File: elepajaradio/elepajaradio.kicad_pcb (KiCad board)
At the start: 2 copper layers, 29 parts, among them J1 SPI, J2 UART, J3 vdd_gnd, J4 reset, SW1 RotaryEncoder, SW2 SW_Push, SW3 SW_Push, U1 MAX2606, U2 OLED_I2C, U3 ATmega328PB-A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

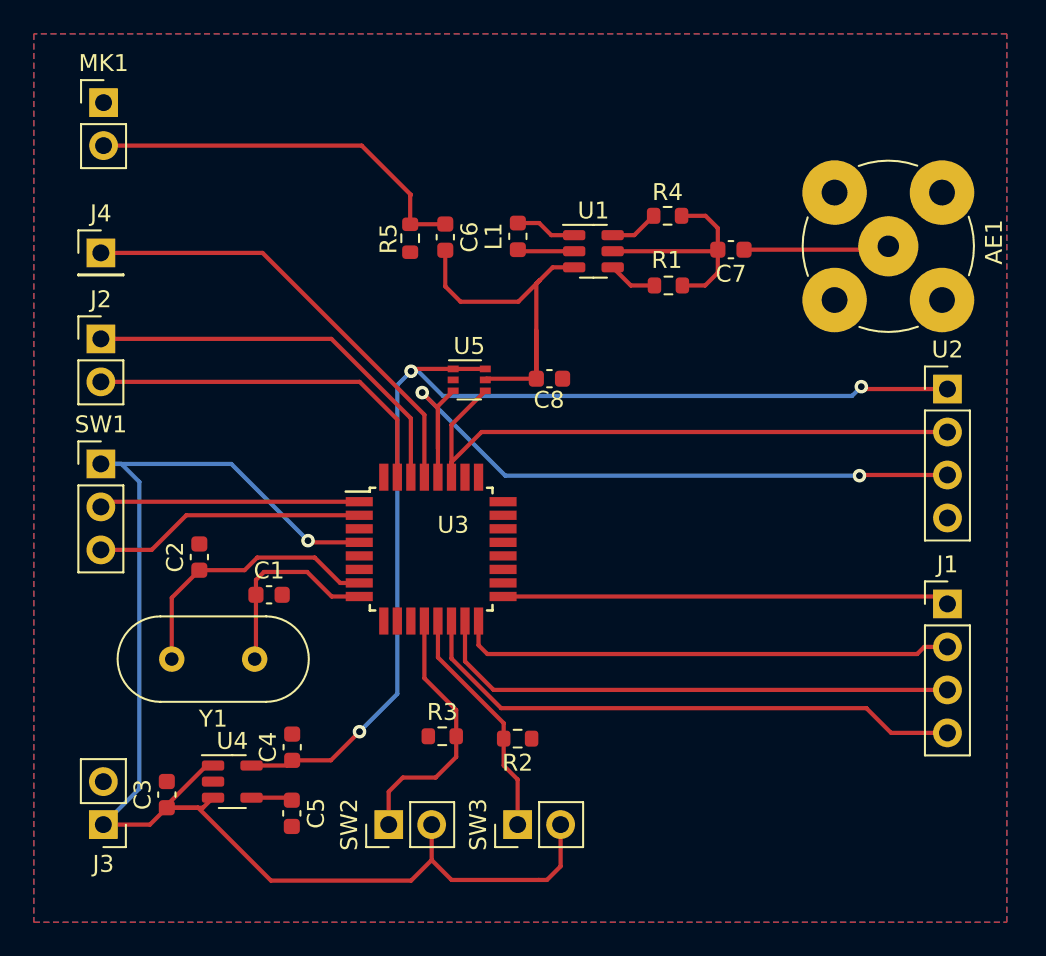
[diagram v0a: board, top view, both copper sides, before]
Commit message: resized transmission line for pcb
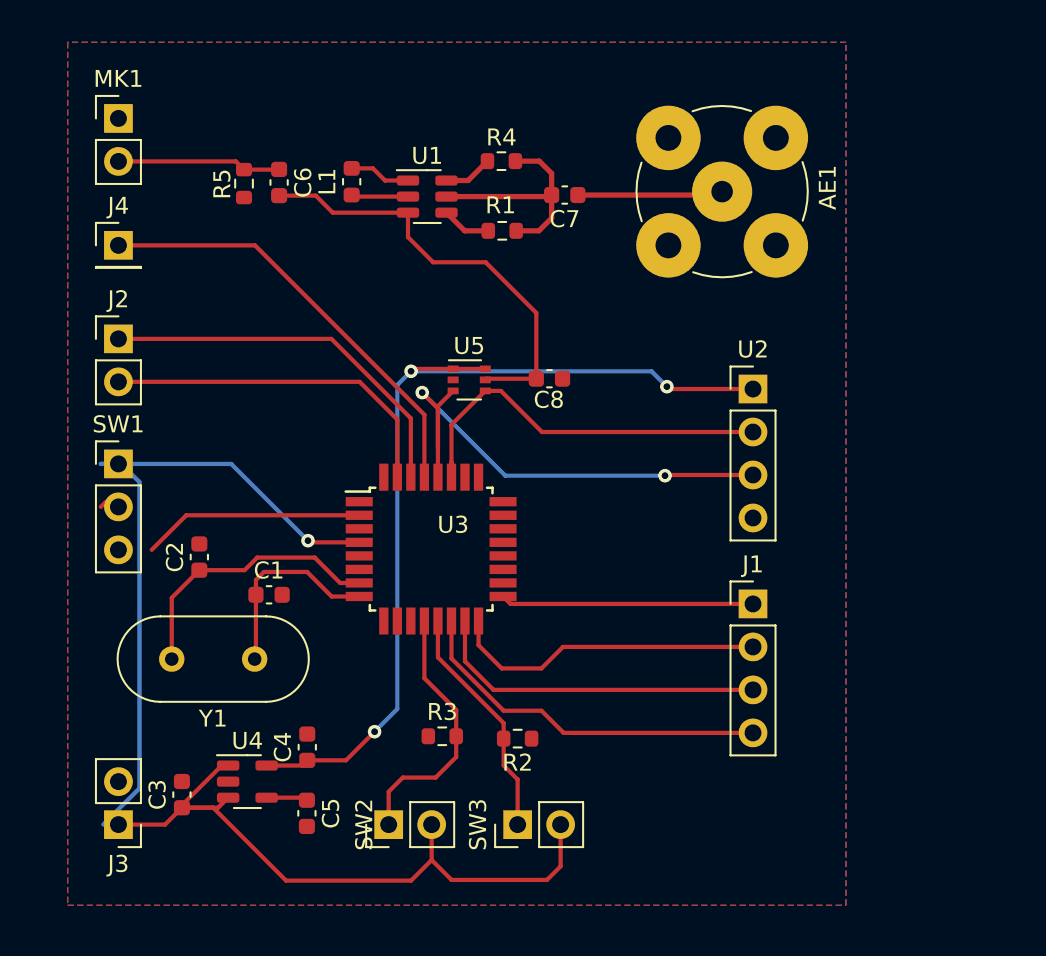
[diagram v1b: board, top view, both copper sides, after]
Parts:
- moved J1 11.5 mm to (162.5, 101.2)
- moved U2 11.5 mm to (162.5, 88.5)
- moved C7 10.3 mm to (151.4, 77.0)
- moved R4 10.3 mm to (147.6, 75.0)
- moved R5 10.3 mm to (132.4, 76.3)
- moved AE1 10.3 mm to (160.7, 76.8)
- moved C6 10.3 mm to (134.5, 76.3)
- moved L1 10.3 mm to (138.8, 76.2)
- moved R1 10.3 mm to (147.7, 79.1)
- moved U1 10.3 mm to (143.2, 77.1)
- moved MK1 1.28 mm to (125.0, 72.5)
- moved J4 1.13 mm to (125.0, 80.0)
- moved J2 1.04 mm to (125.0, 85.5)
- moved SW1 1.04 mm to (125.0, 92.9)
- moved C3 0.89 mm to (128.8, 112.5)
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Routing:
- net Net-(U3-PD3): track 15.4 -> 0.43 mm
- net Net-(MK1-+): track 23.2 -> 9.70 mm
- net SDA0: track 36.9 -> 23.6 mm
- net +3.3V: track 66.8 -> 54.9 mm
- net Net-(J1-Pin_3): track 31.6 -> 20.1 mm
- net SCL0: track 42.2 -> 30.8 mm
- net Net-(J1-Pin_4): track 33.3 -> 21.9 mm
- net Net-(J1-Pin_1): track 26.4 -> 15.6 mm
- net Net-(J1-Pin_2): track 29.5 -> 18.7 mm
- net Net-(U1-TUNE): track 22.8 -> 25.8 mm
- net Net-(U3-PD4): track 16.1 -> 13.1 mm
- net Net-(J2-Pin_2): track 21.9 -> 20.8 mm
- net Net-(J2-Pin_1): track 23.7 -> 22.7 mm
- net VDD: track 83.0 -> 82.1 mm
- net Net-(J4-Pin_1): track 26.8 -> 25.9 mm

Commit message: sized transmission line v2
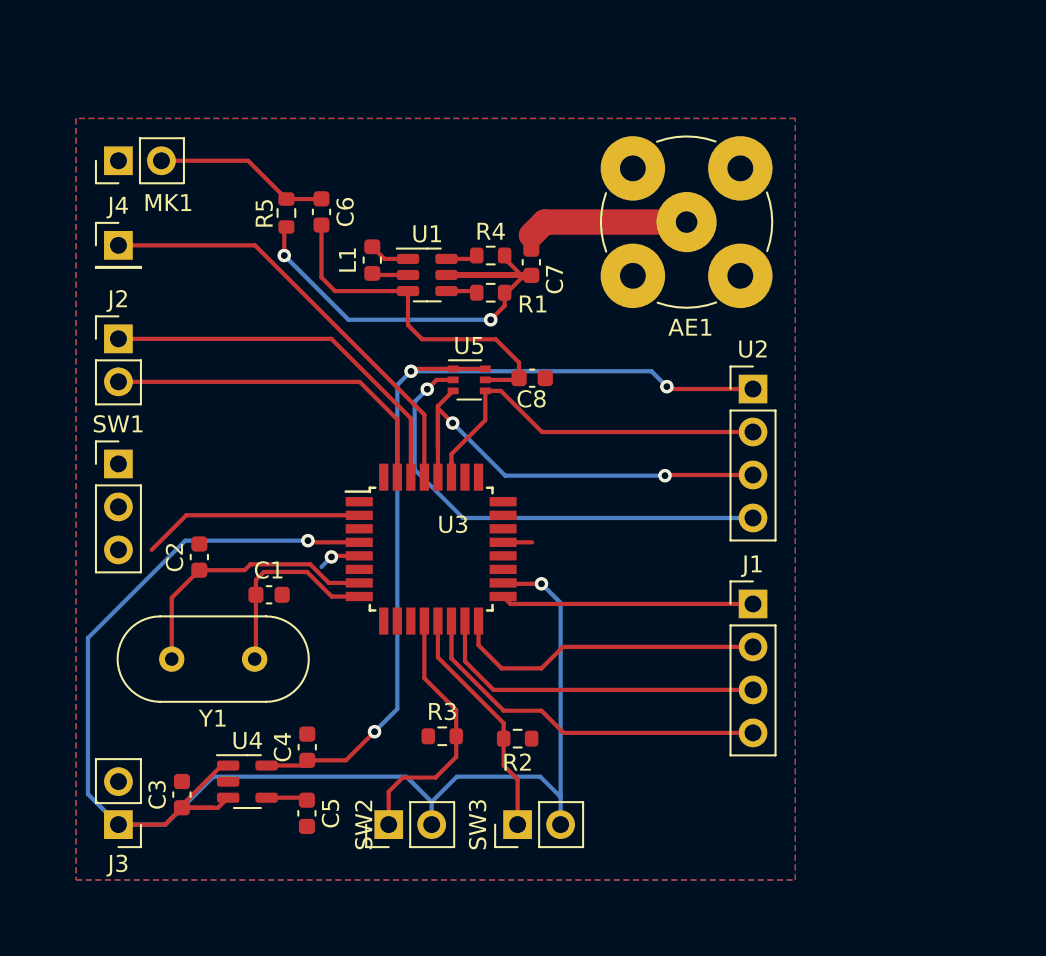
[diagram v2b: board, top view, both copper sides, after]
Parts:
- C1, C2: value C -> 22p
- C3: value C -> 1u
- C4, C6: value C -> 2u2
- C5: value C -> 100p
- C7, C8: value C -> 1n
- L1: value L -> 390n
- R1, R4: value R_US -> 1k
- R2, R3: value R_US -> 10k
- R5: value R_US -> 2k2
- moved R4 5.61 mm to (147.0, 80.6)
- moved L1 4.79 mm to (140.0, 80.9)
- moved U1 4.63 mm to (143.2, 81.8)
- moved C7 4.44 mm to (149.4, 81.0), turned to -90 degrees
- moved R1 3.72 mm to (147.0, 82.8)
- moved C6 3.05 mm to (137.0, 78.0)
- moved R5 3.05 mm to (134.9, 78.1)
- moved AE1 2.77 mm to (158.6, 78.6), turned to 180 degrees
- moved MK1 2.50 mm to (125.0, 75.0), turned to 90 degrees
- moved C8 1.02 mm to (149.4, 87.8)
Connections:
- SW1 pad 1: VDD -> (no net)
- U3 pad 18: unconnected-(U3-AVCC-Pad18) -> VDD
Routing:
- net GND: track 3.37 -> 34.4 mm, vias 0 -> 2
- net 3V3: track 13.7 -> 30.3 mm, vias 0 -> 2
- net VDD: track 82.1 -> 90.4 mm, vias 1 -> 2
- net Net-(U1-TUNE): track 25.8 -> 21.1 mm
- net SCL0: track 30.8 -> 28.6 mm
- net Net-(AE1-A): track 8.61 -> 10.4 mm
- net Net-(U1-IND): track 3.62 -> 2.41 mm
- net Net-(U1-OUT-): track 2.91 -> 1.83 mm
- net Net-(U1-OUT+): track 2.90 -> 1.87 mm
- net Net-(MK1-+): track 9.70 -> 10.4 mm

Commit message: adding PCB gbr and drl files
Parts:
- U5: value MCP4018-xxxxLT -> MCP4018
- moved R1 2.08 mm to (146.2, 80.9)
- moved L1 2.06 mm to (139.3, 78.9)
- moved U1 2.06 mm to (142.5, 79.8)
- moved R4 2.02 mm to (146.2, 78.8)
- moved AE1 1.22 mm to (158.9, 79.8)
- moved C7 1.16 mm to (149.4, 79.8), turned to 180 degrees
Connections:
- SW1 pad 1: (no net) -> VDD
- SW1 pad 2: (no net) -> Net-(U3-PD3)
- SW1 pad 3: (no net) -> Net-(U3-PD4)
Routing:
- net Net-(U3-PD3): track 0.00 -> 14.4 mm
- net VDD: track 90.4 -> 102.1 mm
- net 3V3: track 30.3 -> 24.3 mm
- net Net-(U3-PD4): track 13.1 -> 15.1 mm
- net Net-(AE1-A): track 10.4 -> 8.73 mm
- net Net-(U1-TUNE): track 21.1 -> 21.8 mm
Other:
- board outline added: 45 x 47 mm

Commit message: fixes on new branch for 3v3 node
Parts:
- U5: value MCP4018 -> MCP4018-xxxxLT
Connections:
- C4 pad 1: +3.3V -> 3V3
- SW1 pad 1: VDD -> (no net)
- SW1 pad 2: Net-(U3-PD3) -> (no net)
- SW1 pad 3: Net-(U3-PD4) -> (no net)
- U2 pad 1: +3.3V -> 3V3
- U4 pad 5: +3.3V -> 3V3
- U5 pad 1: +3.3V -> 3V3
- U5 pad 6: +3.3V -> 3V3
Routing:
- net 3V3: track 24.3 -> 89.6 mm, vias 2 -> 5
- net +3.3V: track 54.9 -> 0.00 mm, vias 3 -> 0

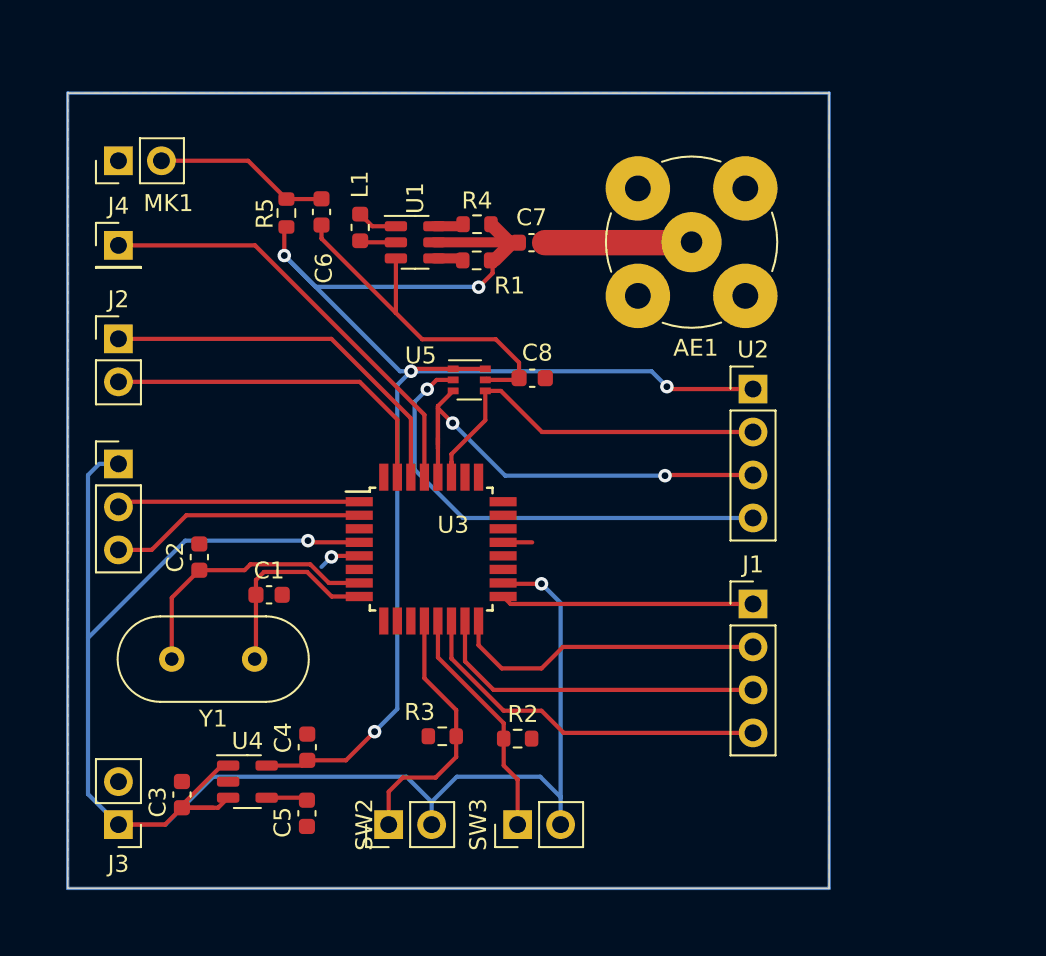
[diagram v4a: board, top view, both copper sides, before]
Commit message: fixing vco output nodes
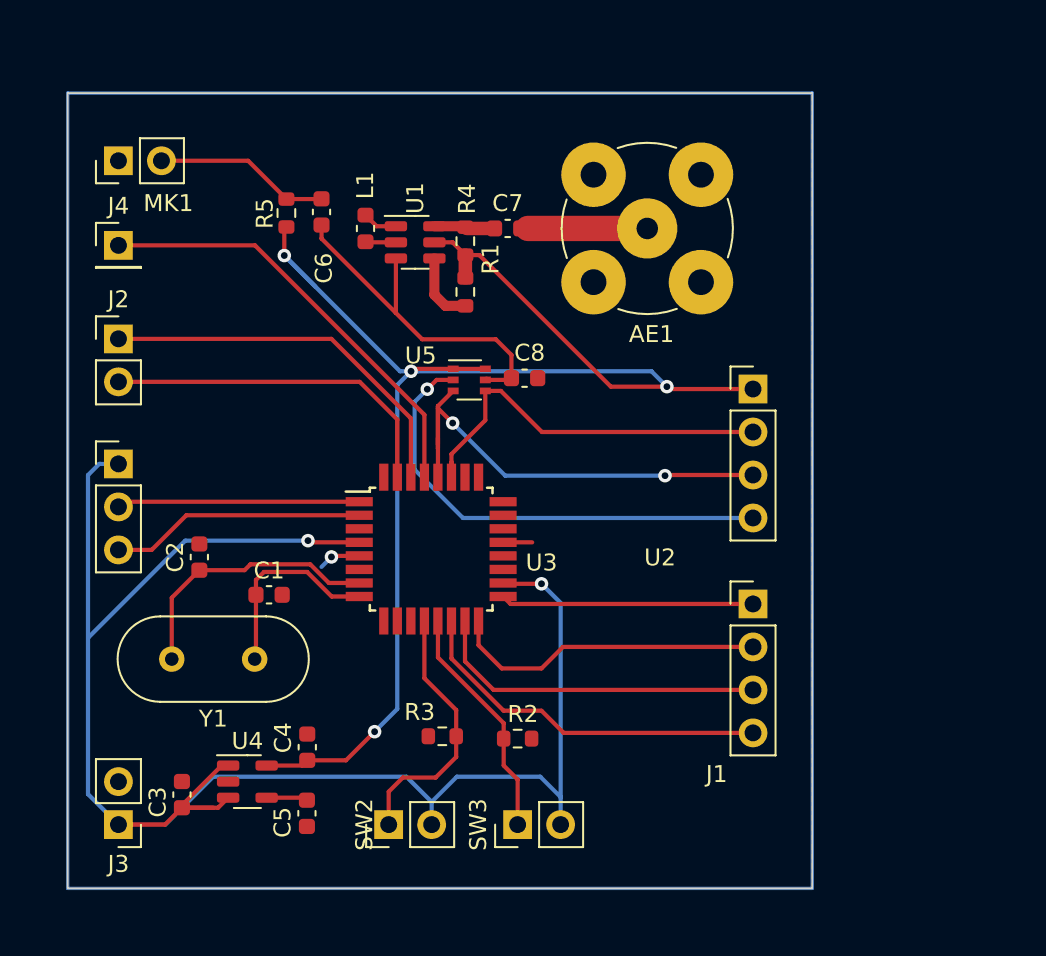
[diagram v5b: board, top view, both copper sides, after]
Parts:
- U5: value MCP4018-xxxxLT -> MCP4018
- moved AE1 2.74 mm to (156.2, 79.0)
- moved R1 1.98 mm to (145.5, 82.8), turned to -90 degrees
- moved C7 1.64 mm to (148.0, 79.0)
- moved R4 1.21 mm to (145.5, 79.8), turned to 90 degrees
- moved C8 0.45 mm to (149.0, 87.8)
- moved L1 0.32 mm to (139.6, 79.0)
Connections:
- AE1 pad 2: (no net) -> GND
- C7 pad 2: 3V3 -> Net-(U1-OUT+)
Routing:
- net Net-(U1-OUT-): track 1.83 -> 4.25 mm
- net Net-(U1-OUT+): track 1.87 -> 3.61 mm
- net Net-(AE1-A): track 8.73 -> 7.06 mm
- net 3V3: track 89.6 -> 88.2 mm, vias 5 -> 4
- net Net-(U1-TUNE): track 21.8 -> 21.2 mm
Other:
- board size 45 x 47 mm -> 44 x 47 mm

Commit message: schematic updates for documentation
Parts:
- removed U2: OLED_I2C, Connector_PinHeader_2.54mm:PinHeader_1x04_P2.54mm_Vertical
- added J5: OLED, Connector_PinHeader_2.54mm:PinHeader_1x04_P2.54mm_Vertical, F.Cu at (162.5, 96.0)
- U5: value MCP4018 -> MCP4018-xxxxLT
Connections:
- net Net-(U3-PB0) renamed B1
- net Net-(U3-PB1) renamed B2
- net Net-(U3-XTAL1/PB6) renamed XTAL1
- net Net-(U3-XTAL2/PB7) renamed XTAL2
- AE1 pad 2: GND -> (no net)
- SW1 pad 1: (no net) -> VDD
- SW1 pad 2: (no net) -> RE1
- SW1 pad 3: (no net) -> RE2
- U3 pad 1: Net-(U3-PD3) -> RE1
- U3 pad 2: Net-(U3-PD4) -> RE2
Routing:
- net RE2: track 0.00 -> 15.1 mm
- net Net-(U3-PD4): track 15.1 -> 0.00 mm
- net RE1: track 0.00 -> 14.4 mm
- net Net-(U3-PD3): track 14.4 -> 0.00 mm
- net SCL0: track 28.6 -> 27.6 mm

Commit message: updates for second order
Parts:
- AE1: footprint Connector_Coaxial:BNC_TEConnectivity_1478204_Vertical -> Connector_Coaxial:SMA_Amphenol_901-143_Horizontal
- moved AE1 2.50 mm to (153.8, 79.0), turned to -90 degrees
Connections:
- AE1 pad 2: (no net) -> GND
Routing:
- net GND: track 34.0 -> 7.79 mm
- net Net-(AE1-A): track 7.06 -> 4.56 mm
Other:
- board text added: "Miikka Elmo Visa"
- board text added: "{dblquote}Sopiva pituus on minimipituus jaettuna kahdella{dblquote}"
